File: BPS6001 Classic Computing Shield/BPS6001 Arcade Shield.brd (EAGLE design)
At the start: 95.2 x 53.3 mm, 46 parts, among them J1 CON_PS/2, J2 CON_PS/2, J3 AUDIO-CONNECTOR-6P-SMD-344003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, U1 AMEGA_SHIELD_NOANALOGNO_ANALOG

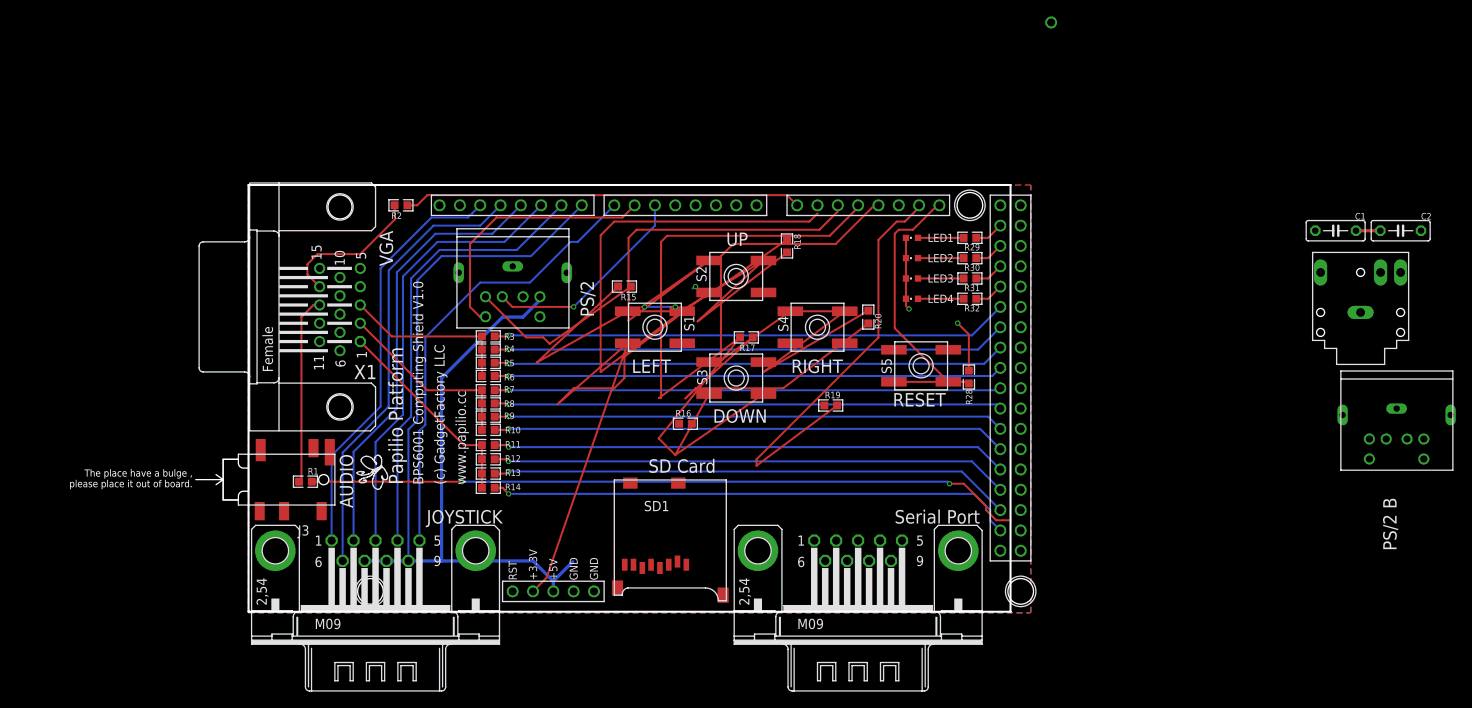
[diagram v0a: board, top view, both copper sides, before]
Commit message: Rearrange with VGA closer to pins
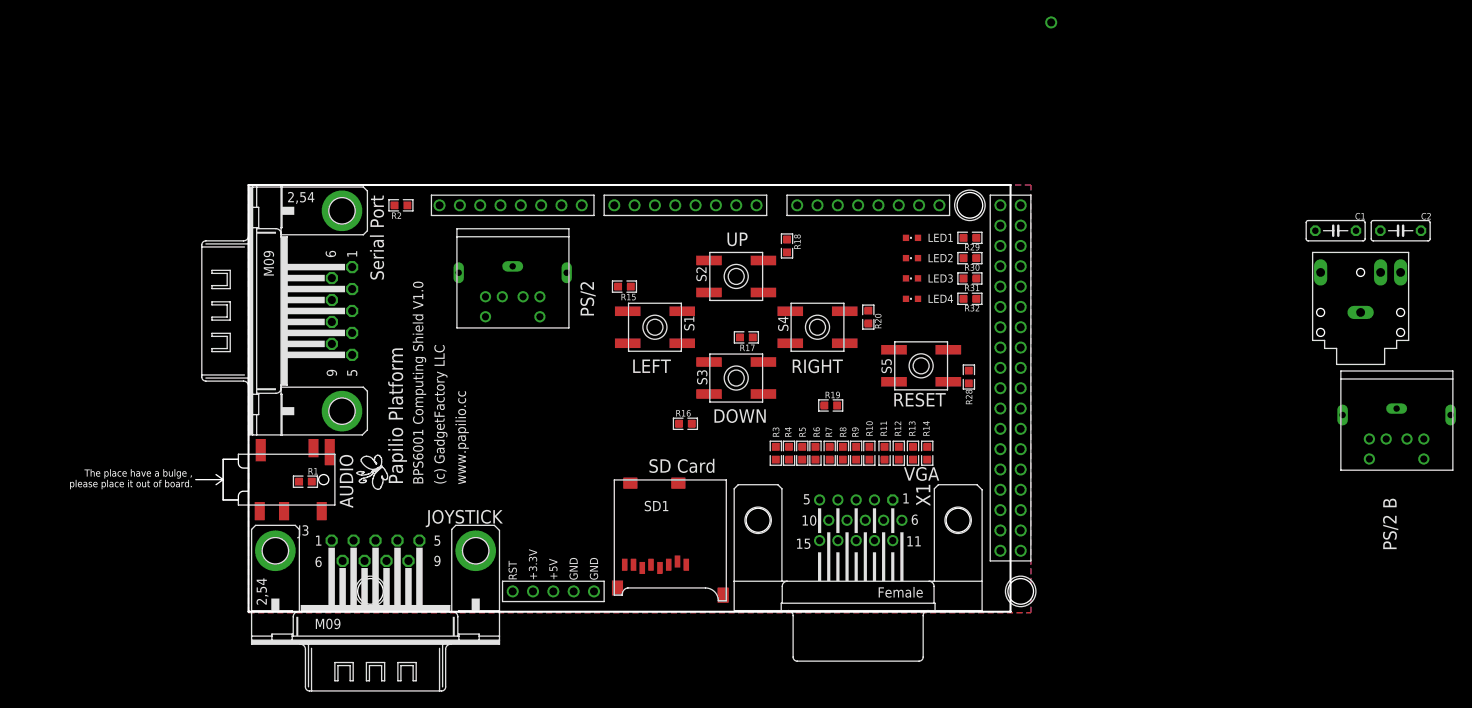
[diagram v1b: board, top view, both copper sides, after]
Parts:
- moved JS2 71.1 mm to (11.7, 37.6), turned to 270 degrees
- moved X1 70.0 mm to (76.2, 11.4), turned to 0 degrees
- moved R14 55.0 mm to (84.8, 19.8), turned to 270 degrees
- moved R13 53.1 mm to (83.1, 19.8), turned to 270 degrees
- moved R12 51.3 mm to (81.3, 19.8), turned to 270 degrees
- moved R11 49.5 mm to (79.5, 19.8), turned to 270 degrees
- moved R10 47.7 mm to (77.6, 19.8), turned to 270 degrees
- moved R9 46.2 mm to (75.9, 19.8), turned to 270 degrees
- moved R8 44.8 mm to (74.3, 19.8), turned to 270 degrees
- moved R7 43.4 mm to (72.6, 19.8), turned to 270 degrees
- moved R6 42.0 mm to (70.9, 19.8), turned to 270 degrees
- moved R5 40.8 mm to (69.2, 19.8), turned to 270 degrees
- moved R4 39.8 mm to (67.6, 19.8), turned to 270 degrees
- moved R3 38.8 mm to (65.9, 19.8), turned to 270 degrees
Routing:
- net SW2: track 103.9 -> 0.00 mm, vias 2 -> 0
- net SW3: track 100.1 -> 0.00 mm
- net GND: track 94.2 -> 0.00 mm, vias 3 -> 0
- net SW1: track 91.8 -> 0.00 mm
- net HORIZONTAL_SYNC: track 89.6 -> 0.00 mm, vias 2 -> 0
- net SW4: track 79.9 -> 0.00 mm
- net 3V3: track 70.7 -> 0.00 mm
- net 5V0: track 69.0 -> 0.00 mm
- net RED1: track 66.2 -> 0.00 mm, vias 1 -> 0
- net RED2: track 65.3 -> 0.00 mm, vias 1 -> 0
- net RED3: track 64.8 -> 0.00 mm, vias 1 -> 0
- net BLUE1: track 64.7 -> 0.00 mm, vias 1 -> 0
- net RED4: track 64.7 -> 0.00 mm, vias 1 -> 0
- net BLUE2: track 64.4 -> 0.00 mm, vias 1 -> 0
- net GREEN4: track 64.3 -> 0.00 mm, vias 1 -> 0
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
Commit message: Move Serial port away from edge
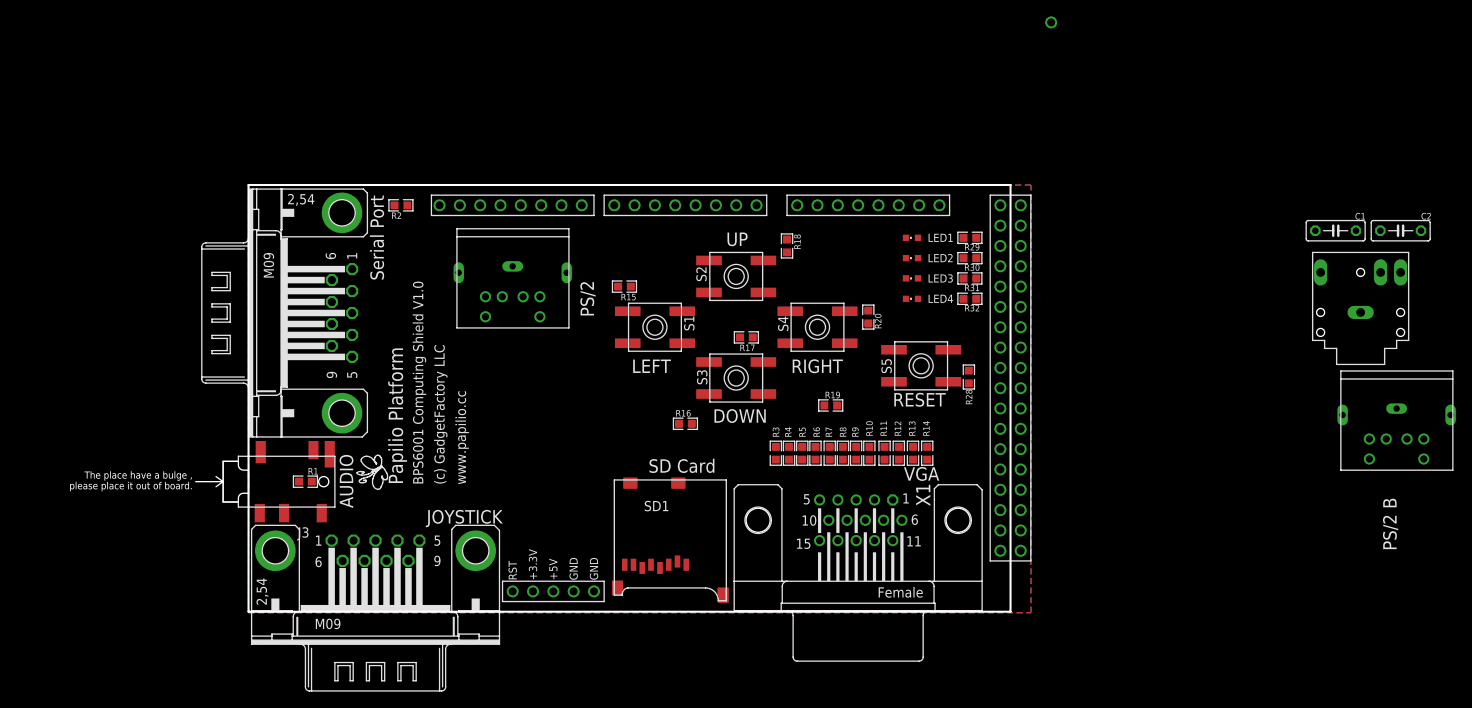
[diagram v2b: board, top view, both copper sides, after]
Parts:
- moved J3 0.25 mm to (3.81, 16.3)
- moved JS2 0.25 mm to (11.7, 37.3)
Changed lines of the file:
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@@
 <grid distance="0.05" unitdist="inch" unit="inch" style="lines" multiple="1" display="no" altdistance="0.01" altunitdist="inch" altunit="inch"/>
 <layers>
-<layer number="1" name="Top" color="4" fill="1" visible="yes" active="yes"/>
+<layer number="1" name="Top" color="4" fill="1" visible="no" active="yes"/>
 <layer number="2" name="Route2" color="1" fill="3" visible="no" active="no"/>
 <layer number="3" name="Route3" color="4" fill="3" visible="no" active="no"/>
 <layer number="14" name="Route14" color="1" fill="6" visible="no" active="no"/>
 <layer number="15" name="Route15" color="4" fill="6" visible="no" active="no"/>
-<layer number="16" name="Bottom" color="1" fill="1" visible="yes" active="yes"/>
+<layer number="16" name="Bottom" color="1" fill="1" visible="no" active="yes"/>
 <layer number="17" name="Pads" color="2" fill="1" visible="yes" active="yes"/>
 <layer number="18" name="Vias" color="2" fill="1" visible="yes" active="yes"/>
-<layer number="19" name="Unrouted" color="12" fill="1" visible="yes" active="yes"/>
+<layer number="19" name="Unrouted" color="12" fill="1" visible="no" active="yes"/>
 <layer number="20" name="Dimension" color="15" fill="1" visible="yes" active="yes"/>
 <layer number="21" name="tPlace" color="25" fill="1" visible="yes" active="yes"/>
 <layer number="22" name="bPlace" color="13" fill="1" visible="yes" active="yes"/>
 <layer number="23" name="tOrigins" color="15" fill="1" visible="yes" active="yes"/>
-<layer number="24" name="bOrigins" color="15" fill="1" visible="yes" active="yes"/>
+<layer number="24" name="bOrigins" color="15" fill="1" visible="no" active="yes"/>
 <layer number="25" name="tNames" color="7" fill="1" visible="yes" active="yes"/>
 <layer number="26" name="bNames" color="7" fill="1" visible="no" active="yes"/>
@@
 <layer number="29" name="tStop" color="7" fill="3" visible="no" active="yes"/>
 <layer number="30" name="bStop" color="7" fill="6" visible="no" active="yes"/>
-<layer number="31" name="tCream" color="7" fill="4" visible="no" active="yes"/>
+<layer number="31" name="tCream" color="7" fill="4" visible="yes" active="yes"/>
 <layer number="32" name="bCream" color="7" fill="5" visible="no" active="yes"/>
 <layer number="33" name="tFinish" color="6" fill="3" visible="no" active="yes"/>
@@
 <layer number="37" name="tTest" color="7" fill="1" visible="no" active="yes"/>
 <layer number="38" name="bTest" color="7" fill="1" visible="no" active="yes"/>
-<layer number="39" name="tKeepout" color="4" fill="11" visible="yes" active="yes"/>
-<layer number="40" name="bKeepout" color="1" fill="11" visible="yes" active="yes"/>
-<layer number="41" name="tRestrict" color="4" fill="10" visible="yes" active="yes"/>
-<layer number="42" name="bRestrict" color="1" fill="10" visible="yes" active="yes"/>
-<layer number="43" name="vRestrict" color="2" fill="10" visible="yes" active="yes"/>
+<layer number="39" name="tKeepout" color="4" fill="11" visible="no" active="yes"/>
+<layer number="40" name="bKeepout" color="1" fill="11" visible="no" active="yes"/>
+<layer number="41" name="tRestrict" color="4" fill="10" visible="no" active="yes"/>
+<layer number="42" name="bRestrict" color="1" fill="10" visible="no" active="yes"/>
+<layer number="43" name="vRestrict" color="2" fill="10" visible="no" active="yes"/>
 <layer number="44" name="Drills" color="7" fill="1" visible="no" active="yes"/>
 <layer number="45" name="Holes" color="7" fill="1" visible="yes" active="yes"/>
@@
 <attribute name="VALUE" x="132.461" y="44.831" size="1.27" layer="27" ratio="10"/>
 </element>
-<element name="JS2" library="con-subd" package="M09HP" value="" x="11.684" y="37.592" smashed="yes" rot="R270">
-<attribute name="VALUE" x="-8.763" y="45.212" size="1.778" layer="27" ratio="10" rot="R270"/>
-<attribute name="MF" value="" x="11.684" y="37.592" size="1.778" layer="27" rot="R270" display="off"/>
-<attribute name="MPN" value="" x="11.684" y="37.592" size="1.778" layer="27" rot="R270" display="off"/>
-<attribute name="OC_FARNELL" value="unknown" x="11.684" y="37.592" size="1.778" layer="27" rot="R270" display="off"/>
-<attribute name="OC_NEWARK" value="unknown" x="11.684" y="37.592" size="1.778" layer="27" rot="R270" display="off"/>
+<element name="JS2" library="con-subd" package="M09HP" value="" x="11.684" y="37.338" smashed="yes" rot="R270">
+<attribute name="VALUE" x="-8.763" y="44.958" size="1.778" layer="27" ratio="10" rot="R270"/>
+<attribute name="MF" value="" x="11.684" y="37.338" size="1.778" layer="27" rot="R270" display="off"/>
+<attribute name="MPN" value="" x="11.684" y="37.338" size="1.778" layer="27" rot="R270" display="off"/>
+<attribute name="OC_FARNELL" value="unknown" x="11.684" y="37.338" size="1.778" layer="27" rot="R270" display="off"/>
+<attribute name="OC_NEWARK" value="unknown" x="11.684" y="37.338" size="1.778" layer="27" rot="R270" display="off"/>
 </element>
 <element name="JS1" library="con-subd" package="M09HP" value="" x="15.875" y="7.62" smashed="yes">
@@
 <element name="U1" library="Papilio" package="AMEGA_SHIELD_NOANALOG" value="AMEGA_SHIELD_NOANALOGNO_ANALOG" x="0" y="0"/>
 <element name="SD1" library="adafruit" package="MICROSD" value="MICROSD" x="45.72" y="16.51"/>
-<element name="J3" library="OPL Eagle Library" package="6P-SMD-3.5" value="AUDIO-CONNECTOR-6P-SMD-3440030P1" x="3.81" y="16.51" rot="R180"/>
+<element name="J3" library="OPL Eagle Library" package="6P-SMD-3.5" value="AUDIO-CONNECTOR-6P-SMD-3440030P1" x="3.81" y="16.256" rot="R180"/>
 </elements>
 <signals>
@@
 <contactref element="U1" pad="RX"/>
 <contactref element="JS2" pad="5"/>
-<wire x1="12.954" y1="32.1056" x2="63.5" y2="50.8" width="0" layer="19" extent="1-1"/>
+<wire x1="12.954" y1="31.8516" x2="63.5" y2="50.8" width="0" layer="19" extent="1-1"/>
 </signal>
 <signal name="TX">
 <contactref element="U1" pad="TX"/>
 <contactref element="JS2" pad="4"/>
-<wire x1="12.954" y1="34.8488" x2="60.96" y2="50.8" width="0" layer="19" extent="1-1"/>
+<wire x1="12.954" y1="34.5948" x2="60.96" y2="50.8" width="0" layer="19" extent="1-1"/>
 </signal>
 <signal name="N$1">
 <contactref element="R16" pad="1"/>
 <contactref element="J3" pad="L"/>
-<wire x1="8.128" y1="20.447" x2="53.81" y2="23.495" width="0" layer="19" extent="1-1"/>
+<wire x1="8.128" y1="20.193" x2="53.81" y2="23.495" width="0" layer="19" extent="1-1"/>
 </signal>
 <signal name="N$2">
 <contactref element="R19" pad="1"/>
 <contactref element="J3" pad="R"/>
-<wire x1="4.445" y1="12.573" x2="71.971" y2="25.781" width="0" layer="19" extent="1-1"/>
+<wire x1="4.445" y1="12.319" x2="71.971" y2="25.781" width="0" layer="19" extent="1-1"/>
 </signal>
 </signals>
